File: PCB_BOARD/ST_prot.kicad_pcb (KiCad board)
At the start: 2 copper layers, 41 x 36 mm, 28 parts, among them J1 USB_B_Micro, J2 Conn_01x15, J3 Conn_01x15, SW2 SW_Push, U1 XC6206P332MR, U2 STM32F103C8T6, Y1 8MHz

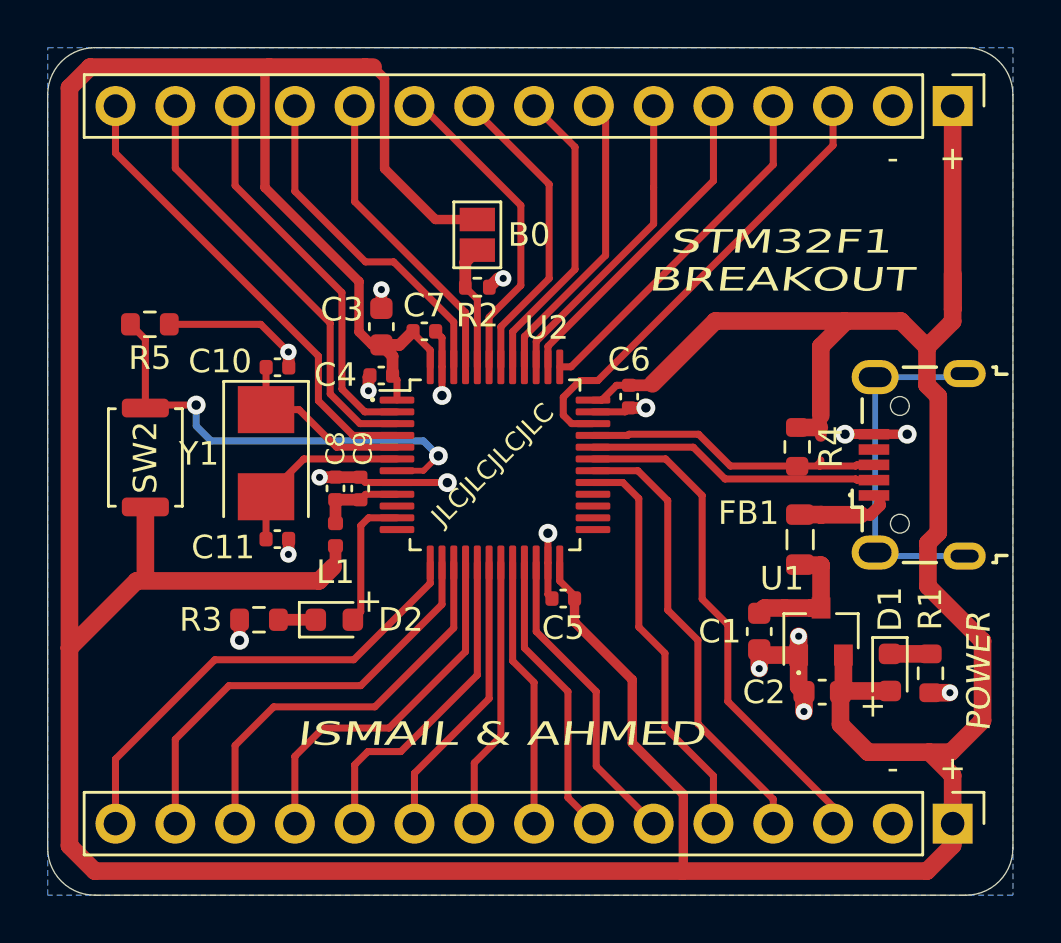
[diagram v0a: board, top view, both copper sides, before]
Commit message: Edit footprint and reroute pcb
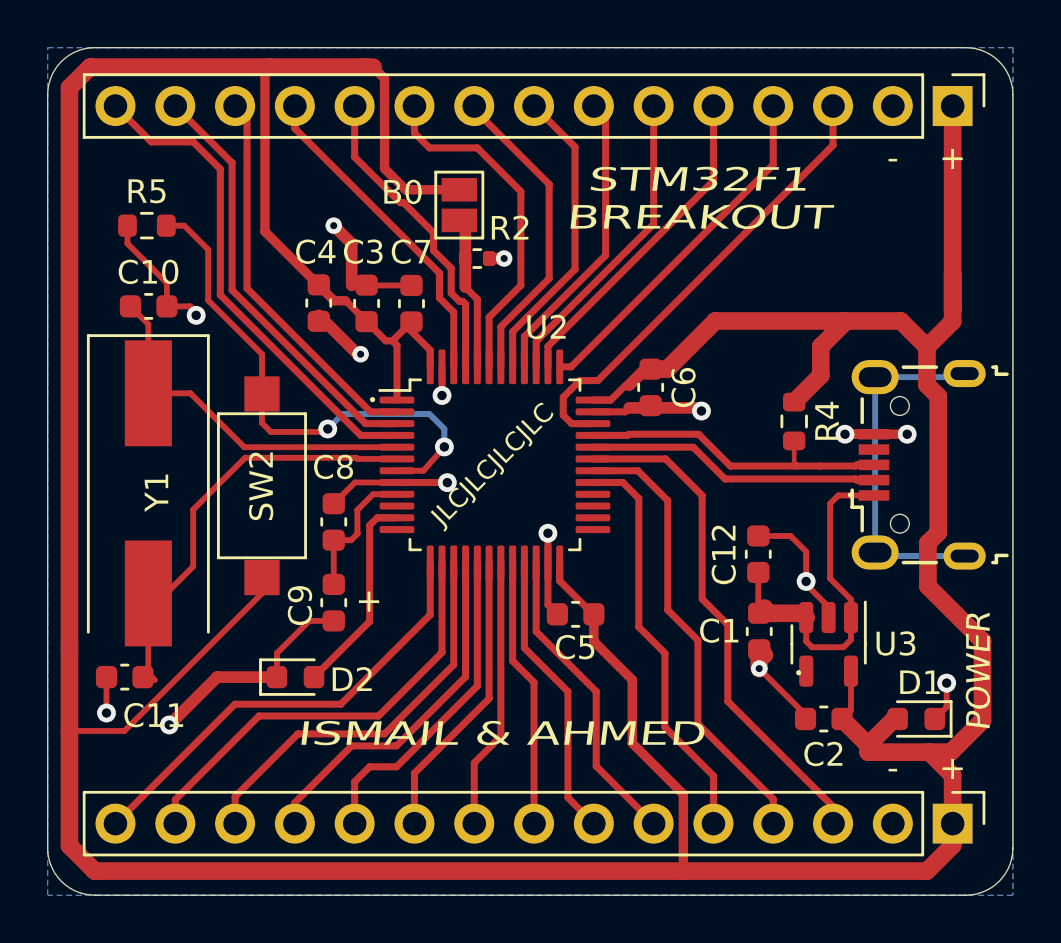
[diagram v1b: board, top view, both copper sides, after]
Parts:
- removed FB1: 100R, Inductor_SMD:L_0805_2012Metric
- removed L1: 27n, Inductor_SMD:L_0402_1005Metric
- removed R1, R3: 1k5, Resistor_SMD:R_0603_1608Metric
- removed U1: XC6206P332MR, Package_TO_SOT_SMD:SOT-23
- added C12: 1u, Capacitor_SMD:C_0603_1608Metric, F.Cu at (83.2, 49.5)
- added U3: XC6210B332MR, Package_TO_SOT_SMD:SOT-23-5, F.Cu at (86.2, 53.3)
- C10, C11, C4, C5, C6, C7, C8, C9: footprint Capacitor_SMD:C_0402_1005Metric -> Capacitor_SMD:C_0603_1608Metric
- SW2: footprint Button_Switch_SMD:SW_Push_SPST_NO_Alps_SKRK -> Button_Switch_SMD:SW_SPST_CK_RS282G05A3
- Y1: footprint Crystal:Crystal_SMD_5032-2Pin_5.0x3.2mm -> Crystal:Crystal_SMD_HC49-SD
- moved C11 8.74 mm to (56.3, 54.7), turned to 180 degrees
- moved C10 6.05 mm to (57.3, 39.0)
- moved Y1 5.28 mm to (57.3, 46.9)
- moved SW2 5.10 mm to (62.1, 46.6)
- moved C9 4.98 mm to (65.2, 51.6), turned to -90 degrees
- moved R5 4.19 mm to (57.2, 35.6), turned to 0 degrees
- moved C4 4.06 mm to (64.5, 38.8), turned to -90 degrees
- moved D2 2.94 mm to (63.5, 54.7)
- moved D1 2.27 mm to (89.9, 56.5), turned to 180 degrees
- moved JP1 1.48 mm to (70.5, 34.7)
- moved C8 1.43 mm to (65.2, 48.1)
- moved C7 1.30 mm to (68.5, 38.9), turned to 90 degrees
- moved R2 1.22 mm to (71.2, 37.0)
- moved C3 1.17 mm to (66.5, 38.9)
- moved C2 1.14 mm to (86.0, 56.5)
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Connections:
- C1 pad 1: VCC -> +5V
- D1 pad 1: Net-(D1-K) -> GND
- D2 pad 1: Net-(D2-K) -> GND
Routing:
- net GND: track 34.0 -> 55.1 mm, vias 17 -> 15
- net +5V: track 4.00 -> 15.4 mm
- net /HSE_IN: track 8.03 -> 18.3 mm
- net +3.3V: track 213.9 -> 204.2 mm
- net /HSE_OUT: track 8.03 -> 15.5 mm
- net VCC: track 5.83 -> 0.00 mm
- net /LED_STAT: track 5.81 -> 8.72 mm
- net Net-(U2-NRST): track 19.8 -> 22.3 mm
- net +3.3VA: track 3.71 -> 5.98 mm
- net Net-(D1-K): track 1.72 -> 0.00 mm
- net Net-(D2-K): track 1.59 -> 0.00 mm
- net /BOOT0: track 5.38 -> 6.54 mm
- net PB7: track 13.7 -> 14.7 mm
- net PC15: track 20.0 -> 20.9 mm
- net PA3: track 20.1 -> 19.3 mm
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
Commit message: Finish prototype v1 PCB
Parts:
- C1: footprint Capacitor_SMD:C_0603_1608Metric -> Capacitor_SMD:C_0603_1608Metric_Pad1.08x0.95mm_HandSolder
- moved C6 6.39 mm to (84.7, 40.5)
- moved D2 4.27 mm to (67.8, 54.7)
- moved C12 3.60 mm to (84.6, 52.8), turned to -90 degrees
- moved C5 2.93 mm to (78.3, 52.3)
- moved U2 2.32 mm to (74.3, 45.6)
- moved C9 1.98 mm to (67.1, 51.0)
- moved C8 1.95 mm to (67.1, 47.7)
- moved U3 1.73 mm to (87.8, 53.9)
- moved R2 1.53 mm to (72.6, 37.6)
- moved JP1 1.49 mm to (71.9, 35.2)
- moved C2 1.29 mm to (87.0, 57.3)
- moved C1 1.06 mm to (82.2, 52.8)
- moved D1 0.92 mm to (90.4, 57.3)
- moved C11 0.86 mm to (57.1, 54.7)
- moved SW2 0.25 mm to (62.4, 46.6)
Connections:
- C8 pad 1: +3.3VA -> +3.3V
- C9 pad 1: +3.3VA -> +3.3V
- U2 pad 9: +3.3VA -> +3.3V
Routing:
- net GND: track 55.1 -> 67.2 mm, vias 15 -> 11
- net +3.3V: track 204.2 -> 215.0 mm
- net +3.3VA: track 5.98 -> 0.00 mm
- net PA3: track 19.3 -> 23.9 mm
- net PA7: track 13.9 -> 17.2 mm
- net PB0: track 12.4 -> 15.4 mm
- net PA4: track 18.7 -> 21.7 mm
- net PA6: track 15.2 -> 18.0 mm
- net PA5: track 17.1 -> 19.8 mm
- net /HSE_OUT: track 15.5 -> 18.2 mm
- net Net-(U2-NRST): track 22.3 -> 19.9 mm
- net USB_D+: track 14.6 -> 12.3 mm
- net USB_D-: track 12.8 -> 10.5 mm
- net PC15: track 20.9 -> 23.2 mm
- net PC13: track 16.5 -> 18.8 mm
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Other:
- board text added: "STM32F1-V1 PROTOTYOPE"
- board text removed: "B0"
- board text removed: "STM32F1 BREAKOUT"
